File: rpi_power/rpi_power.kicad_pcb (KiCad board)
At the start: 2 copper layers, 69 x 57.4 mm, 68 parts, among them J1 POWER, J2 Raspberry_Pi_2_3, J3 Raspberry_Pi_2_3, J4 ADC, J7 PROG, J9 GPIO, Q10 IRLML6344TRPBF, Q6 IRLML6344TRPBF, U1 TPS54625, U2 ATxmega16A4U-AU, U3 LM2936-3.3, Y1 Crystal

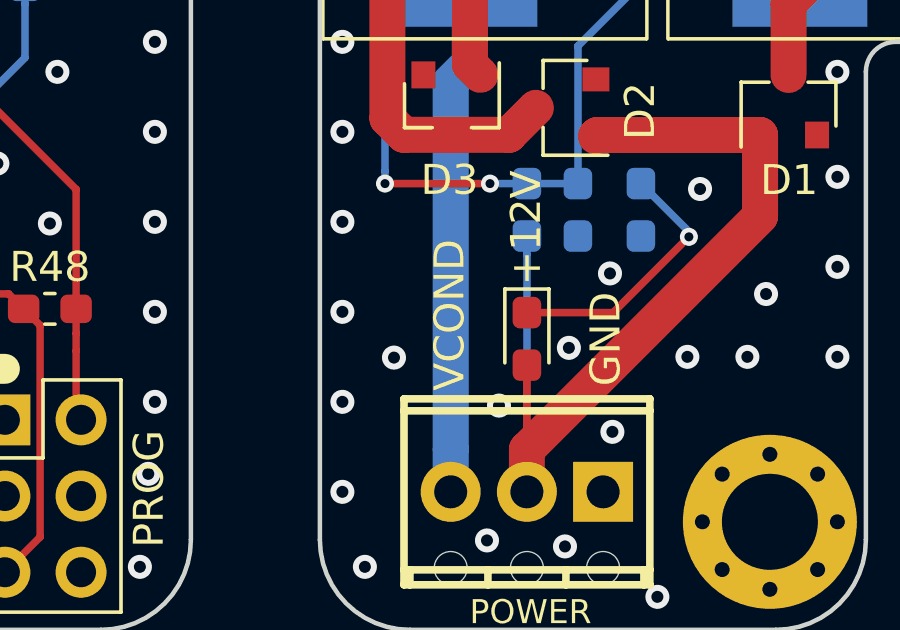
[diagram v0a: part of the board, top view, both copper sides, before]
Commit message: Corrected silkscreen.
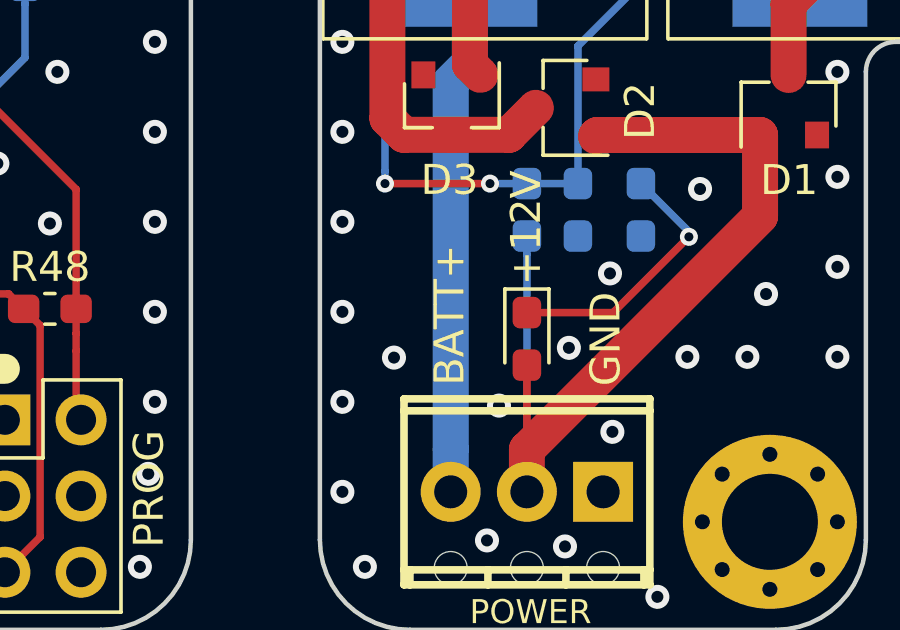
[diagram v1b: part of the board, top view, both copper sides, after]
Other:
- board text added: "BATT+"
- board text removed: "VCOND"
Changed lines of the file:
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@@
     (effects (font (size 1 1) (thickness 0.2)))
   )
-  (gr_text VCOND (at 167.322036 113.105421 90) (layer F.SilkS)
+  (gr_text BATT+ (at 167.322036 113.105421 90) (layer F.SilkS)
     (effects (font (size 1 1) (thickness 0.2)))
   )
@@
   (gr_line (start 137.22 72.02) (end 137.72 72.02) (layer Dwgs.User) (width 0.2))
   (gr_line (start 129.7 72.12) (end 130 72.12) (layer Dwgs.User) (width 0.2))
-  (segment (start 168.5 89.5) (end 168 90) (width 1.2) (layer B.Cu) (net 67) (status 30))
-  (segment (start 168.5 84.25) (end 168.5 89.5) (width 1.2) (layer B.Cu) (net 67) (status 30))
-  (segment (start 166.499999 97.399999) (end 168 98.9) (width 1.2) (layer B.Cu) (net 67))
-  (segment (start 166.499999 94.400001) (end 166.499999 97.399999) (width 1.2) (layer B.Cu) (net 67))
-  (segment (start 168 92.9) (end 166.499999 94.400001) (width 1.2) (layer B.Cu) (net 67))
-  (segment (start 168 90) (end 168 92.9) (width 1.2) (layer B.Cu) (net 67) (status 10))
-  (segment (start 168 98.9) (end 168 101.8) (width 1.2) (layer B.Cu) (net 67) (status 20))
-  (via (at 168 98.9) (size 1) (drill 0.7) (layers F.Cu B.Cu) (net 67))
-  (segment (start 168 104.75) (end 168.35 105.1) (width 1.2) (layer F.Cu) (net 67) (status 30))
-  (segment (start 168 98.9) (end 168 104.75) (width 1.2) (layer F.Cu) (net 67) (status 20))
   (segment (start 168.5 95.75) (end 180 95.75) (width 1.2) (layer F.Cu) (net 1) (status 30))
   (via (at 151.8 84.155421) (size 1) (drill 0.7) (layers F.Cu B.Cu) (net 2) (status 30))
@@
   (segment (start 133.615918 116.905918) (end 135.71 119) (width 0.25) (layer F.Cu) (net 35) (status 20))
   (segment (start 133.615918 111.39574) (end 133.615918 116.905918) (width 0.25) (layer F.Cu) (net 35) (status 10))
-  (segment (start 144.375 103.15) (end 144.3 103.075) (width 0.25) (layer B.Cu) (net 68) (status 30))
-  (via (at 136 101.6) (size 0.6) (drill 0.3) (layers F.Cu B.Cu) (net 68))
-  (segment (start 136 100.011658) (end 136.015918 99.99574) (width 0.25) (layer F.Cu) (net 68) (status 30))
-  (segment (start 136 101.6) (end 136 100.011658) (width 0.25) (layer F.Cu) (net 68) (status 20))
-  (segment (start 146.225 103.075) (end 146.3 103.15) (width 0.25) (layer B.Cu) (net 68) (status 30))
-  (segment (start 144.3 103.075) (end 146.225 103.075) (width 0.25) (layer B.Cu) (net 68) (status 30))
-  (segment (start 142.825 101.6) (end 144.3 103.075) (width 0.25) (layer B.Cu) (net 68) (status 20))
-  (segment (start 136 101.6) (end 142.825 101.6) (width 0.25) (layer B.Cu) (net 68))
   (segment (start 123.280168 78.905168) (end 128.636302 78.905168) (width 0.25) (layer B.Cu) (net 36) (status 20))
   (segment (start 120.875 76.5) (end 123.280168 78.905168) (width 0.25) (layer B.Cu) (net 36) (status 10))
@@
   (segment (start 124.87 73.52) (end 124.87 71.225) (width 0.25) (layer B.Cu) (net 66))
   (segment (start 124.87 71.225) (end 124.87 73.525) (width 0.25) (layer F.Cu) (net 66))
+  (segment (start 168.5 89.5) (end 168 90) (width 1.2) (layer B.Cu) (net 67) (status 30))
+  (segment (start 168.5 84.25) (end 168.5 89.5) (width 1.2) (layer B.Cu) (net 67) (status 30))
+  (segment (start 166.499999 97.399999) (end 168 98.9) (width 1.2) (layer B.Cu) (net 67))
+  (segment (start 166.499999 94.400001) (end 166.499999 97.399999) (width 1.2) (layer B.Cu) (net 67))
+  (segment (start 168 92.9) (end 166.499999 94.400001) (width 1.2) (layer B.Cu) (net 67))
+  (segment (start 168 90) (end 168 92.9) (width 1.2) (layer B.Cu) (net 67) (status 10))
+  (segment (start 168 98.9) (end 168 101.8) (width 1.2) (layer B.Cu) (net 67) (status 20))
+  (via (at 168 98.9) (size 1) (drill 0.7) (layers F.Cu B.Cu) (net 67))
+  (segment (start 168 104.75) (end 168.35 105.1) (width 1.2) (layer F.Cu) (net 67) (status 30))
+  (segment (start 168 98.9) (end 168 104.75) (width 1.2) (layer F.Cu) (net 67) (status 20))
   (segment (start 167.36 117.585787) (end 167.36 119) (width 1.2) (layer B.Cu) (net 67) (status 20))
   (segment (start 167.36 105.34) (end 167.36 117.585787) (width 1.2) (layer B.Cu) (net 67))
@@
   (segment (start 158.04 97.43359) (end 158.5886 96.88499) (width 0.25) (layer B.Cu) (net 67))
   (segment (start 158.04 98.079933) (end 158.04 97.43359) (width 0.25) (layer B.Cu) (net 67))
+  (segment (start 144.375 103.15) (end 144.3 103.075) (width 0.25) (layer B.Cu) (net 68) (status 30))
+  (via (at 136 101.6) (size 0.6) (drill 0.3) (layers F.Cu B.Cu) (net 68))
+  (segment (start 136 100.011658) (end 136.015918 99.99574) (width 0.25) (layer F.Cu) (net 68) (status 30))
+  (segment (start 136 101.6) (end 136 100.011658) (width 0.25) (layer F.Cu) (net 68) (status 20))
+  (segment (start 146.225 103.075) (end 146.3 103.15) (width 0.25) (layer B.Cu) (net 68) (status 30))
+  (segment (start 144.3 103.075) (end 146.225 103.075) (width 0.25) (layer B.Cu) (net 68) (status 30))
+  (segment (start 142.825 101.6) (end 144.3 103.075) (width 0.25) (layer B.Cu) (net 68) (status 20))
+  (segment (start 136 101.6) (end 142.825 101.6) (width 0.25) (layer B.Cu) (net 68))
   (zone (net 8) (net_name +5V) (layer F.Cu) (hatch edge 0.508)
     (priority 2)
